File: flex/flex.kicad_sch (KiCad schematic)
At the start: 103 parts, among them J1 NA_Conn_01x06_Female, J2 NA_Conn_01x05_Female, J3 NA_Conn_01x06_Female, J4 NA_Conn_01x03_Female, J5 NA_Conn_01x03_Female, SW1 SW_Push, SW10 SW_Push, SW11 SW_Push, SW12 SW_Push, SW13 SW_Push, SW14 SW_Push, SW15 SW_Push, SW16 SW_Push, SW17 SW_Push, SW18 SW_Push, SW19 SW_Push, SW2 SW_Push, SW20 SW_Push, SW21 SW_Push, SW22 SW_Push, SW23 SW_Push, SW24 SW_Push, SW3 SW_Push, SW4 SW_Push, SW5 SW_Push, SW6 SW_Push, SW7 SW_Push, SW8 SW_Push, SW9 SW_Push

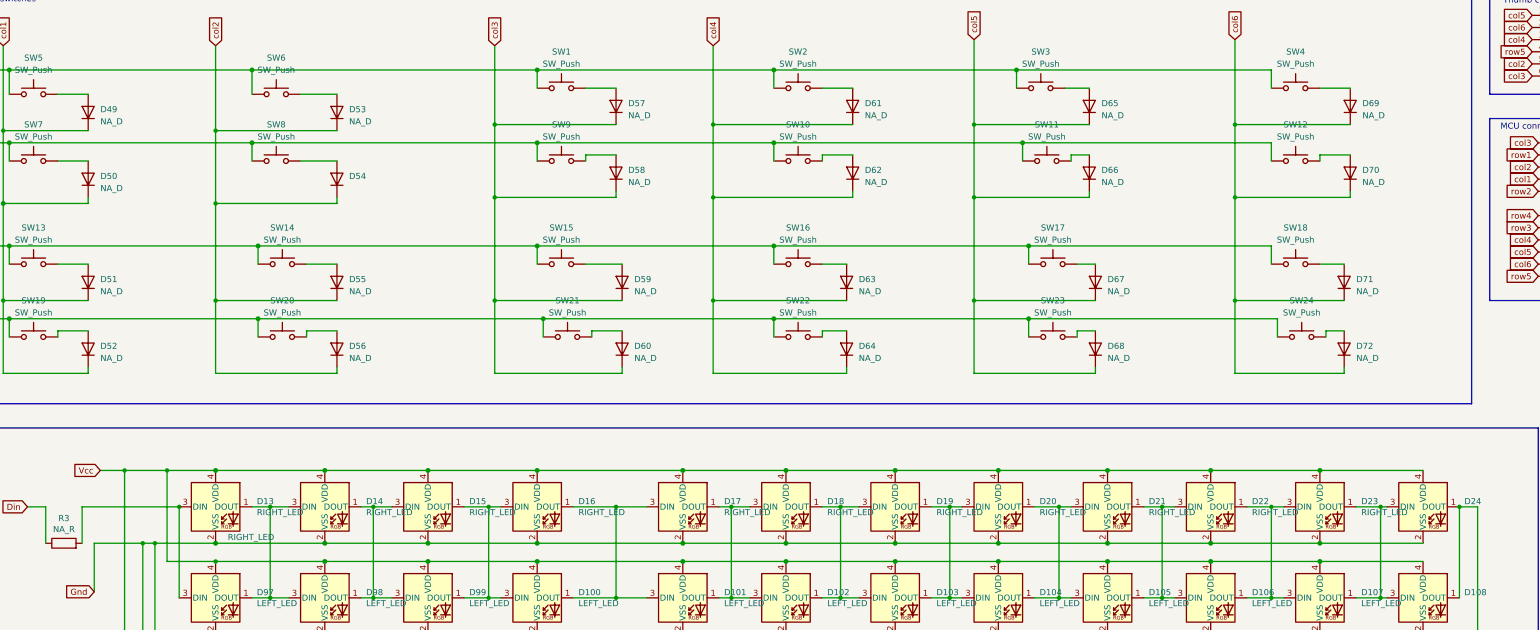
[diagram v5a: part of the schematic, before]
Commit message: diodes horizontal, more space for RGB
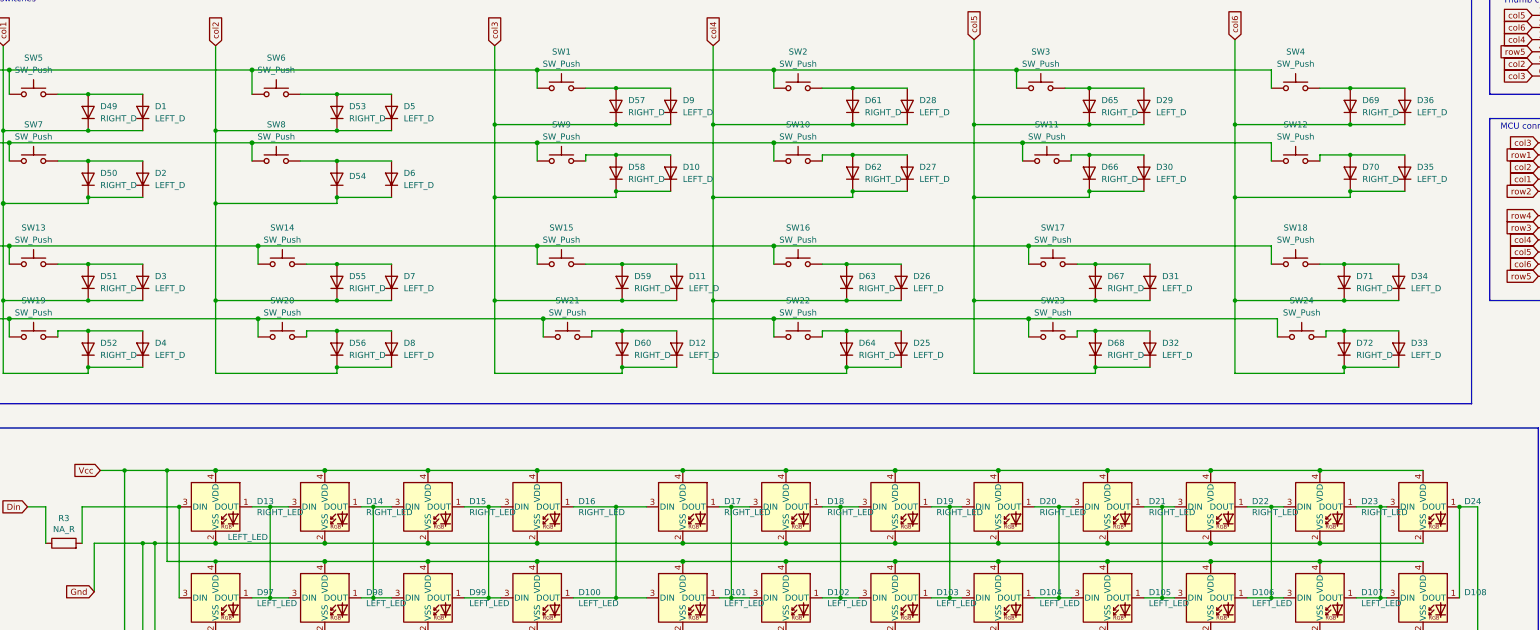
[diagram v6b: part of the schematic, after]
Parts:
- added D1, D10, D11, D12, D2, D25, D26, D27, D28, D29, D3, D30, D31, D32, D33, D34, D35, D36, D4, D5, D6, D7, D8, D9: LEFT_D, customs:SOD123_assembly, symbol Diode:1N4148
- D108: value RIGHT_LED -> LEFT_LED
- D49, D50, D51, D52, D53, D54, D55, D56, D57, D58, D59, D60, D61, D62, D63, D64, D65, D66, D67, D68, D69, D70, D71, D72: value NA_D -> RIGHT_D; footprint custom:Diode_TH_SOD123 -> customs:SOD123_assembly
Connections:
- net col1: now also D1.1 (K), D2.1 (K), D3.1 (K), D4.1 (K)
- net col2: now also D5.1 (K), D6.1 (K), D7.1 (K), D8.1 (K)
- net col3: now also D10.1 (K), D11.1 (K), D12.1 (K), D9.1 (K)
- net col4: now also D25.1 (K), D26.1 (K), D27.1 (K), D28.1 (K)
- net col5: now also D29.1 (K), D30.1 (K), D31.1 (K), D32.1 (K)
- net col6: now also D33.1 (K), D34.1 (K), D35.1 (K), D36.1 (K)
- net at D50.2 (A), SW7.2: now also D2.2 (A)
- net at D68.2 (A), SW23.2: now also D32.2 (A)
- net at D61.2 (A), SW2.2: now also D28.2 (A)
- net at D53.2 (A), SW6.2: now also D5.2 (A)
- net at D59.2 (A), SW15.2: now also D11.2 (A)
- net at D56.2 (A), SW20.2: now also D8.2 (A)
- net at D66.2 (A), SW11.2: now also D30.2 (A)
- net at D60.2 (A), SW21.2: now also D12.2 (A)
- net at D55.2 (A), SW14.2: now also D7.2 (A)
- net at D67.2 (A), SW17.2: now also D31.2 (A)
- net at D54.2 (A), SW8.2: now also D6.2 (A)
- net at D49.2 (A), SW5.2: now also D1.2 (A)
- net at D51.2 (A), SW13.2: now also D3.2 (A)
- net at D70.2 (A), SW12.2: now also D35.2 (A)
- net at D52.2 (A), SW19.2: now also D4.2 (A)
- net at D71.2 (A), SW18.2: now also D34.2 (A)
- net at D64.2 (A), SW22.2: now also D25.2 (A)
- net at D57.2 (A), SW1.2: now also D9.2 (A)
- net at D62.2 (A), SW10.2: now also D27.2 (A)
- net at D65.2 (A), SW3.2: now also D29.2 (A)
- net at D58.2 (A), SW9.2: now also D10.2 (A)
- net at D69.2 (A), SW4.2: now also D36.2 (A)
- net at D63.2 (A), SW16.2: now also D26.2 (A)
- net at D72.2 (A), SW24.2: now also D33.2 (A)

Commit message: drilled mouse bites
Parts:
- added Mousebite1, Mousebite10, Mousebite11, Mousebite12, Mousebite2, Mousebite3, Mousebite4, Mousebite5, Mousebite6, Mousebite7, Mousebite8, Mousebite9: ~, customs:mousebite, symbol customs:mousebite

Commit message: BOM work
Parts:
- D1, D10, D11, D12, D2, D25, D26, D27, D28, D29, D3, D30, D31, D32, D33, D34, D35, D36, D4, D49, D5, D50, D51, D52, D53, D54, D55, D56, D57, D58, D59, D6, D60, D61, D62, D63, D64, D65, D66, D67, D68, D69, D7, D70, D71, D72, D8, D9: now in the parts list
- D100, D101, D102, D103, D104, D105, D106, D107, D108, D109, D110, D111, D112, D113, D114, D115, D116, D117, D118, D119, D120, D13, D14, D15, D16, D17, D18, D19, D20, D21, D22, D23, D24, D37, D38, D39, D40, D41, D42, D43, D44, D45, D46, D47, D48, D97, D98, D99: LCSC (none) -> C2890035
